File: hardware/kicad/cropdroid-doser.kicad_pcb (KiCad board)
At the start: 2 copper layers, 396.1 x 133.9 mm, 41 parts, among them CON1 SJ1-3523N, CON10 SJ1-3523N, CON2 SJ1-3523N, CON3 SJ1-3523N, CON4 SJ1-3523N, CON5 SJ1-3523N, CON6 SJ1-3523N, CON7 SJ1-3523N, CON8 SJ1-3523N, CON9 SJ1-3523N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

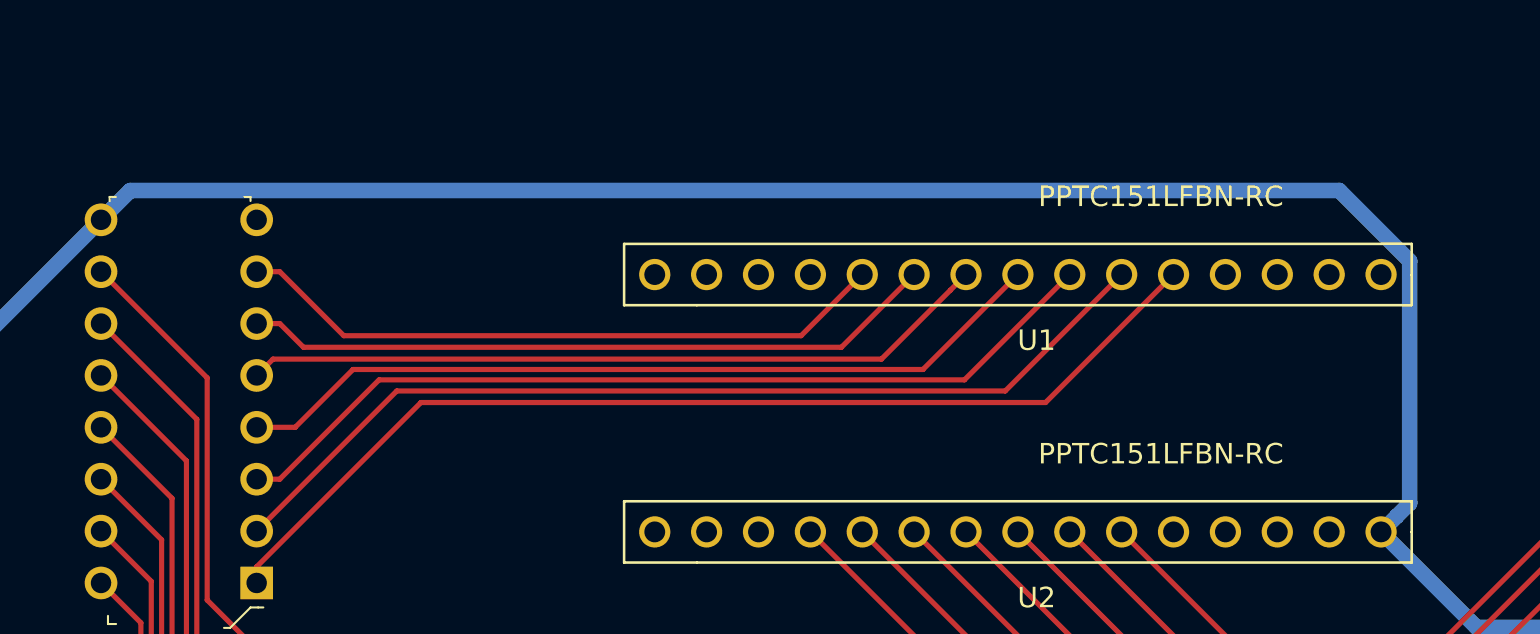
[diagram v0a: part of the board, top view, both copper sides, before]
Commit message: fix kicad nano pinout
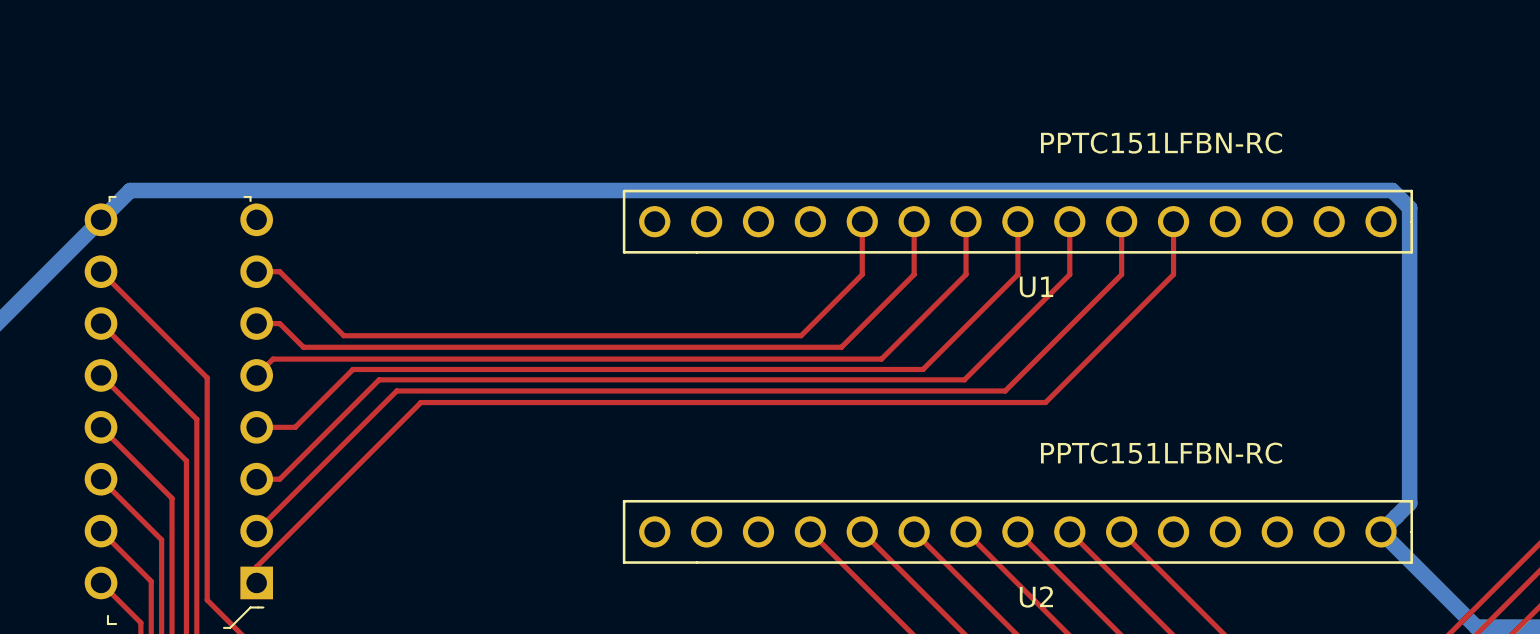
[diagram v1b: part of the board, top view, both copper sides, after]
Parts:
- moved U1 2.59 mm to (100.2, 43.8)
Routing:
- net Net-(Q1-Pad7): track 32.2 -> 34.8 mm
- net Net-(Q1-Pad6): track 34.1 -> 36.7 mm
- net Net-(Q1-Pad5): track 36.8 -> 39.4 mm
- net Net-(Q1-Pad2): track 47.6 -> 50.1 mm
- net Net-(Q1-Pad4): track 40.4 -> 43.0 mm
- net Net-(Q1-Pad3): track 44.0 -> 46.5 mm
- net Net-(Q1-Pad1): track 51.6 -> 54.2 mm
- net Net-(CON1-Pad2): track 651.6 -> 653.1 mm
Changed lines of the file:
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@@
     (thickness 1.6)
     (drawings 19)
-    (tracks 316)
+    (tracks 322)
     (zones 0)
     (modules 41)
@@
   )
   (setup
-    (last_trace_width 0.254)
+    (last_trace_width 0.762)
     (user_trace_width 0.762)
     (user_trace_width 2.794)
@@
     (mod_text_size 1 1)
     (mod_text_width 0.15)
-    (pad_size 4.199999 4.199999)
-    (pad_drill 3.200001)
+    (pad_size 1.53 1.53)
+    (pad_drill 1.02)
     (pad_to_mask_clearance 0.0508)
     (aux_axis_origin 0 0)
@@
   )
   (module PPTC151LFBN-RC:PPTC151LFBN-RC (layer F.Cu)
-    (at 100.2 46.35 180)
+    (at 100.2 43.76166 180)
     (fp_text reference U1 (at 16.8653 -3.22461) (layer F.SilkS)
       (effects (font (size 1.002992 1.002992) (thickness 0.015)))
@@
   (segment (start 104.865001 63.615001) (end 127.284999 63.615001) (width 0.762) (layer B.Cu) (net 2))
   (segment (start 100.2 58.95) (end 104.865001 63.615001) (width 0.762) (layer B.Cu) (net 2))
-  (segment (start 100.964999 58.185001) (end 100.2 58.95) (width 0.762) (layer B.Cu) (net 2))
-  (segment (start 101.600001 57.549999) (end 100.964999 58.185001) (width 0.762) (layer B.Cu) (net 2))
-  (segment (start 101.600001 45.677999) (end 101.600001 57.549999) (width 0.762) (layer B.Cu) (net 2))
-  (segment (start 98.157001 42.234999) (end 101.600001 45.677999) (width 0.762) (layer B.Cu) (net 2))
-  (segment (start 38.965001 42.234999) (end 98.157001 42.234999) (width 0.762) (layer B.Cu) (net 2))
-  (segment (start 37.53 43.67) (end 38.965001 42.234999) (width 0.762) (layer B.Cu) (net 2))
   (segment (start 23.8 57.4) (end 37.53 43.67) (width 0.762) (layer B.Cu) (net 2))
   (segment (start 23.8 137.2) (end 23.8 57.4) (width 0.762) (layer B.Cu) (net 2))
@@
   (segment (start 163.094001 143.314197) (end 166.036 140.372198) (width 0.762) (layer B.Cu) (net 2))
   (segment (start 163.094001 143.435001) (end 163.094001 143.314197) (width 0.762) (layer B.Cu) (net 2))
+  (segment (start 100.964999 58.185001) (end 100.2 58.95) (width 0.762) (layer B.Cu) (net 2))
+  (segment (start 100.745341 42.234999) (end 101.600001 43.089659) (width 0.762) (layer B.Cu) (net 2))
+  (segment (start 101.600001 57.549999) (end 100.964999 58.185001) (width 0.762) (layer B.Cu) (net 2))
+  (segment (start 38.965001 42.234999) (end 100.745341 42.234999) (width 0.762) (layer B.Cu) (net 2))
+  (segment (start 101.600001 43.089659) (end 101.600001 57.549999) (width 0.762) (layer B.Cu) (net 2))
+  (segment (start 37.53 43.67) (end 38.965001 42.234999) (width 0.762) (layer B.Cu) (net 2))
   (segment (start 37.53 58.91) (end 39.989741 61.369741) (width 0.254) (layer F.Cu) (net 5))
   (segment (start 38.08 142.2) (end 36.576 142.2) (width 0.254) (layer F.Cu) (net 5))
@@
   (segment (start 45.15 60.657882) (end 53.191782 52.6161) (width 0.254) (layer F.Cu) (net 39))
   (segment (start 45.15 61.45) (end 45.15 60.657882) (width 0.254) (layer F.Cu) (net 39))
+  (segment (start 53.191782 52.6161) (end 83.7739 52.6161) (width 0.254) (layer F.Cu) (net 39))
+  (segment (start 90.04 46.35) (end 90.04 43.76166) (width 0.254) (layer F.Cu) (net 39))
   (segment (start 83.7739 52.6161) (end 90.04 46.35) (width 0.254) (layer F.Cu) (net 39))
-  (segment (start 53.191782 52.6161) (end 83.7739 52.6161) (width 0.254) (layer F.Cu) (net 39))
   (segment (start 45.15 58.91) (end 52.01032 52.04968) (width 0.254) (layer F.Cu) (net 40))
+  (segment (start 52.01032 52.04968) (end 81.80032 52.04968) (width 0.254) (layer F.Cu) (net 40))
+  (segment (start 87.5 46.35) (end 87.5 43.76166) (width 0.254) (layer F.Cu) (net 40))
   (segment (start 81.80032 52.04968) (end 87.5 46.35) (width 0.254) (layer F.Cu) (net 40))
-  (segment (start 52.01032 52.04968) (end 81.80032 52.04968) (width 0.254) (layer F.Cu) (net 40))
   (segment (start 46.28137 56.37) (end 51.145349 51.506021) (width 0.254) (layer F.Cu) (net 41))
   (segment (start 45.15 56.37) (end 46.28137 56.37) (width 0.254) (layer F.Cu) (net 41))
+  (segment (start 51.145349 51.506021) (end 79.803979 51.506021) (width 0.254) (layer F.Cu) (net 41))
+  (segment (start 84.96 46.35) (end 84.96 43.76166) (width 0.254) (layer F.Cu) (net 41))
   (segment (start 79.803979 51.506021) (end 84.96 46.35) (width 0.254) (layer F.Cu) (net 41))
-  (segment (start 51.145349 51.506021) (end 79.803979 51.506021) (width 0.254) (layer F.Cu) (net 41))
   (segment (start 45.15 53.83) (end 47.03594 53.83) (width 0.254) (layer F.Cu) (net 42))
   (segment (start 47.03594 53.83) (end 49.867929 50.998011) (width 0.254) (layer F.Cu) (net 42))
+  (segment (start 49.867929 50.998011) (end 77.771989 50.998011) (width 0.254) (layer F.Cu) (net 42))
+  (segment (start 82.42 46.35) (end 82.42 43.76166) (width 0.254) (layer F.Cu) (net 42))
   (segment (start 77.771989 50.998011) (end 82.42 46.35) (width 0.254) (layer F.Cu) (net 42))
-  (segment (start 49.867929 50.998011) (end 77.771989 50.998011) (width 0.254) (layer F.Cu) (net 42))
-  (segment (start 79.115001 47.114999) (end 79.88 46.35) (width 0.254) (layer F.Cu) (net 43))
-  (segment (start 75.739999 50.490001) (end 79.115001 47.114999) (width 0.254) (layer F.Cu) (net 43))
   (segment (start 45.949999 50.490001) (end 75.739999 50.490001) (width 0.254) (layer F.Cu) (net 43))
   (segment (start 45.15 51.29) (end 45.949999 50.490001) (width 0.254) (layer F.Cu) (net 43))
+  (segment (start 79.88 46.35) (end 79.88 43.76166) (width 0.254) (layer F.Cu) (net 43))
+  (segment (start 75.739999 50.490001) (end 79.88 46.35) (width 0.254) (layer F.Cu) (net 43))
   (segment (start 46.28137 48.75) (end 47.44237 49.911) (width 0.254) (layer F.Cu) (net 44))
   (segment (start 45.15 48.75) (end 46.28137 48.75) (width 0.254) (layer F.Cu) (net 44))
+  (segment (start 47.44237 49.911) (end 73.779 49.911) (width 0.254) (layer F.Cu) (net 44))
+  (segment (start 77.34 46.35) (end 77.34 43.76166) (width 0.254) (layer F.Cu) (net 44))
   (segment (start 73.779 49.911) (end 77.34 46.35) (width 0.254) (layer F.Cu) (net 44))
-  (segment (start 47.44237 49.911) (end 73.779 49.911) (width 0.254) (layer F.Cu) (net 44))
   (segment (start 46.28137 46.21) (end 49.41595 49.34458) (width 0.254) (layer F.Cu) (net 45))
   (segment (start 45.15 46.21) (end 46.28137 46.21) (width 0.254) (layer F.Cu) (net 45))
+  (segment (start 49.41595 49.34458) (end 71.80542 49.34458) (width 0.254) (layer F.Cu) (net 45))
+  (segment (start 74.8 46.35) (end 74.8 43.76166) (width 0.254) (layer F.Cu) (net 45))
   (segment (start 71.80542 49.34458) (end 74.8 46.35) (width 0.254) (layer F.Cu) (net 45))
-  (segment (start 49.41595 49.34458) (end 71.80542 49.34458) (width 0.254) (layer F.Cu) (net 45))
   (segment (start 121.1 59.64) (end 111.62406 69.11594) (width 0.254) (layer F.Cu) (net 47))
   (segment (start 82.42594 69.11594) (end 72.26 58.95) (width 0.254) (layer F.Cu) (net 47))
